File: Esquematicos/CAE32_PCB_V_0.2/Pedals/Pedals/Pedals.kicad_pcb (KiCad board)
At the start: 2 copper layers, 45 x 55 mm, 16 parts, among them U1 STM32G070RBT6, U2 LDL1117

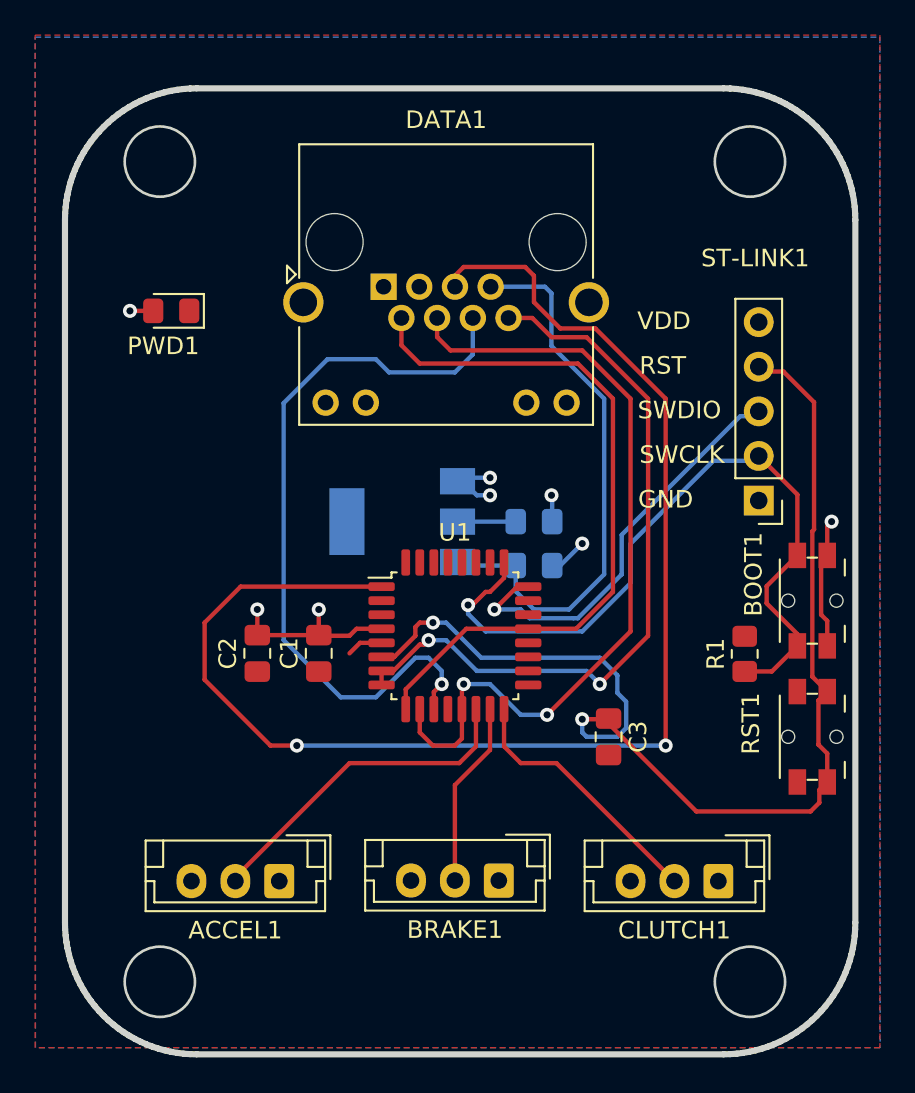
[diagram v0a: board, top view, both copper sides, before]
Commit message: Correciones de errores PCB:pedales y hall
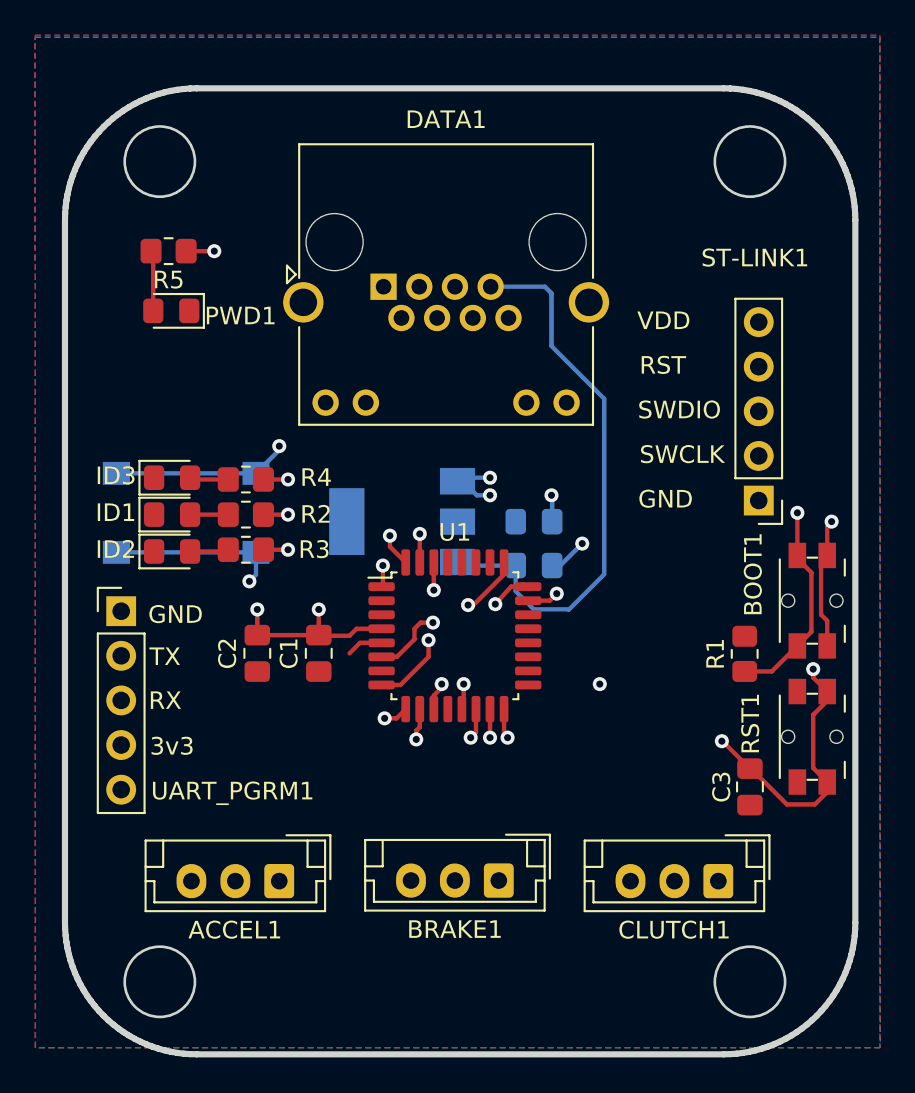
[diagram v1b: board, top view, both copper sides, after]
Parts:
- added ID1: LED, LED_SMD:LED_0805_2012Metric_Pad1.15x1.40mm_HandSolder, F.Cu at (130.4, 96.1)
- added ID2: LED, LED_SMD:LED_0805_2012Metric_Pad1.15x1.40mm_HandSolder, F.Cu at (130.4, 98.2)
- added ID3: LED, LED_SMD:LED_0805_2012Metric_Pad1.15x1.40mm_HandSolder, F.Cu at (130.4, 94.0)
- added MODE1: SW_Push, Button_Switch_SMD:SW_Push_1P1T_NO_6x6mm_H9.5mm, B.Cu at (131.2, 96.0)
- added R2: 10, Resistor_SMD:R_0805_2012Metric_Pad1.20x1.40mm_HandSolder, F.Cu at (134.6, 96.1)
- added R3: 10, Resistor_SMD:R_0805_2012Metric_Pad1.20x1.40mm_HandSolder, F.Cu at (134.6, 98.1)
- added R4: 10, Resistor_SMD:R_0805_2012Metric_Pad1.20x1.40mm_HandSolder, F.Cu at (134.6, 94.1)
- added R5: 43, Resistor_SMD:R_0805_2012Metric_Pad1.20x1.40mm_HandSolder, F.Cu at (130.2, 81.1)
- added UART_PGRM1: Conn_01x05_Female, Connector_PinHeader_2.54mm:PinHeader_1x05_P2.54mm_Vertical, F.Cu at (127.5, 101.6)
- moved C3 8.54 mm to (163.3, 111.6)
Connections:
- DATA1 pad 5: /CS_PROGRAM -> unconnected-(DATA1-Pad5)
- PWD1 pad 2: +3.3V -> Net-(PWD1-Pad2)
- U1 pad 1: /CS_PROGRAM -> /MODE
- U1 pad 10: /MISO -> /USART_RX
- U1 pad 21: /MOSI -> unconnected-(U1-Pad21)
- U1 pad 23: unconnected-(U1-Pad23) -> /MOSI
- U1 pad 30: unconnected-(U1-Pad30) -> /IND0
- U1 pad 31: unconnected-(U1-Pad31) -> /IND1
- U1 pad 32: unconnected-(U1-Pad32) -> /IND2
- U1 pad 7: /SCKL -> unconnected-(U1-Pad7)
- U1 pad 9: /MOSI -> /USART_TX
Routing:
- net /CS_PROGRAM: track 78.6 -> 0.00 mm, vias 2 -> 0
- net /MODE: track 0.00 -> 20.6 mm, vias 0 -> 2
- net /USART_RX: track 0.00 -> 19.5 mm, vias 0 -> 1
- net /IND1: track 0.00 -> 18.8 mm, vias 0 -> 2
- net /USART_TX: track 0.00 -> 17.8 mm, vias 0 -> 1
- net /CS_PDL: track 42.1 -> 24.9 mm
- net /IND0: track 0.00 -> 13.1 mm, vias 0 -> 2
- net /MOSI: track 41.1 -> 30.5 mm, vias 0 -> 1
- net /IND2: track 0.00 -> 10.4 mm, vias 0 -> 2
- net GNDREF: track 10.5 -> 20.2 mm, vias 4 -> 5
- net /NRST: track 66.6 -> 58.3 mm, vias 2 -> 3
- net /MISO: track 46.3 -> 40.5 mm, vias 2 -> 1
- net Net-(PWD1-Pad2): track 0.00 -> 3.45 mm
- net +3.3V: track 22.5 -> 19.4 mm
- net Net-(ID2-Pad2): track 0.00 -> 2.22 mm
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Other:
- copper layers 2 -> 4
- board text added: "3v3"
- board text added: "RX"
- board text added: "TX"

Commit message: Ultima revision de PCBs
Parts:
- added 5V1: TestPoint, TestPoint:TestPoint_Pad_D3.0mm, B.Cu at (158.6, 101.2)
- added GND1: TestPoint, TestPoint:TestPoint_Pad_D3.0mm, B.Cu at (158.4, 106.9)
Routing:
- net GNDREF: track 20.2 -> 28.9 mm, vias 5 -> 8
- net +5V: track 31.6 -> 35.8 mm
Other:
- board text removed: "VDD"

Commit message: reinicio
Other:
- board text added: "5V"
- board text added: "BOOT"
- board text added: "CS"
- board text added: "MISO"
- board text added: "MOSI"
- board text added: "SCKL"
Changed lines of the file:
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@@
   (gr_line (start 169.217804 78.221573) (end 169.263297 78.587814) (layer "Edge.Cuts") (width 0.349999))
   (gr_line (start 125.019113 76.124473) (end 125.18355 75.797418) (layer "Edge.Cuts") (width 0.349999))
+  (gr_text "5V\n" (at 148.75 80.25 90) (layer "B.SilkS")
+    (effects (font (size 1 1) (thickness 0.15)) (justify mirror))
+  )
+  (gr_text "CS" (at 147.6 87.15 90) (layer "B.SilkS")
+    (effects (font (size 1 1) (thickness 0.15)) (justify mirror))
+  )
+  (gr_text "SCKL\n" (at 148.95 87.95 90) (layer "B.SilkS")
+    (effects (font (size 1 1) (thickness 0.15)) (justify mirror))
+  )
+  (gr_text "MISO\n" (at 145.7 88.1 90) (layer "B.SilkS")
+    (effects (font (size 1 1) (thickness 0.15)) (justify mirror))
+  )
+  (gr_text "GND" (at 142.5 79.8 270) (layer "B.SilkS")
+    (effects (font (size 1 1) (thickness 0.15)) (justify mirror))
+  )
+  (gr_text "BOOT" (at 144.6 79.3 270) (layer "B.SilkS")
+    (effects (font (size 1 1) (thickness 0.15)) (justify mirror))
+  )
+  (gr_text "MOSI\n" (at 143.55 88.15 90) (layer "B.SilkS")
+    (effects (font (size 1 1) (thickness 0.15)) (justify mirror))
+  )
   (gr_text "RST" (at 158.333334 87.6125) (layer "F.SilkS")
     (effects (font (size 1 1) (thickness 0.15)))
